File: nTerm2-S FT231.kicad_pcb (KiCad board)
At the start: 2 copper layers, 147.3 x 55.9 mm, 121 parts, among them J1 VGA, J2 Keyboard, J3 Mouse, J4 Line-out/Speaker, J5 RS-232 V.24, J6 USB_C_Receptacle_USB2.0_16P, J7 Line-out/Speaker, K1 IM41 3V, K2 IM41 3V, K3 IM41 3V, Q1 BC817, Q2 BC817, Q3 BC817, Q4 BC817, Q5 BC817, Q6 BC817, Q7 BC817, Q8 BC817, SW1 IO0, SW2 RESET, SW3 DEFAULTS, U1 ESP32-WROOM-32, U2 LM386, U3 MAX3232E, U4 DS2417, U5 NCP1117-3.3_SOT223, U6 USBLC6-2SC6, U7 FT231XS, Y1 32.768MHz

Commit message: Exported library and footprints to project local library for distribution.
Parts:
- C1, C25, C26, C27: footprint Capacitor_SMD:CP_Elec_6.3x7.7 -> Library:CP_Elec_6.3x7.7
- C10, C11, C12, C14, C17, C19, C21, C8, C9: footprint Capacitor_Tantalum_SMD:CP_EIA-3216-18_Kemet-A_Pad1.58x1.35mm_HandSolder -> Library:CP_EIA-3216-18_Kemet-A_Pad1.58x1.35mm_HandSolder
- C13, C18: footprint Capacitor_Tantalum_SMD:CP_EIA-6032-28_Kemet-C_Pad2.25x2.35mm_HandSolder -> Library:CP_EIA-6032-28_Kemet-C_Pad2.25x2.35mm_HandSolder
- C15, C16, C22, C24, C28, C29, C30, C31, C32, C33, C4, C5, C6, C7: footprint Capacitor_SMD:C_0603_1608Metric_Pad1.08x0.95mm_HandSolder -> Library:C_0603_1608Metric_Pad1.08x0.95mm_HandSolder
- C2: footprint Capacitor_SMD:CP_Elec_5x5.4 -> Library:CP_Elec_5x5.4
- C20: footprint Capacitor_Tantalum_SMD:CP_EIA-3528-21_Kemet-B_Pad1.50x2.35mm_HandSolder -> Library:CP_EIA-3528-21_Kemet-B_Pad1.50x2.35mm_HandSolder
- C23: footprint Capacitor_Tantalum_SMD:CP_EIA-7343-30_AVX-N_Pad2.25x2.55mm_HandSolder -> Library:CP_EIA-7343-30_AVX-N_Pad2.25x2.55mm_HandSolder
- C3: footprint Capacitor_SMD:C_0805_2012Metric_Pad1.18x1.45mm_HandSolder -> Library:C_0805_2012Metric_Pad1.18x1.45mm_HandSolder
- D10, D6, D8, D9: footprint Diode_SMD:D_SOD-123 -> Library:D_SOD-123
- D11, D12: footprint Sporos_Tech_Footprints:DIALIGHT_LED_3MM_DOUBLE -> Library:DIALIGHT_LED_3MM_DOUBLE
- D3: footprint Diode_SMD:Nexperia_CFP3_SOD-123W -> Library:Nexperia_CFP3_SOD-123W
- D4: footprint Sporos_Tech_Footprints:DIALIGHT_LED_3MM_SINGLE -> Library:DIALIGHT_LED_3MM_SINGLE
- E1: footprint Sporos_Tech_Footprints:Gold Cap V-Type -> Library:Gold Cap V-Type
- H1, H2, H3, H4, H5, H6: footprint MountingHole:MountingHole_3.2mm_M3 -> Library:MountingHole_3.2mm_M3
- J1: footprint Sporos_Tech_Footprints:DSUB-15-HD_Female_Horizontal_P2.29x1.98mm_EdgePinOffset8.35mm_Housed_MountingHolesOffset10.89mm -> Library:DSUB-15-HD_Female_Horizontal_P2.29x1.98mm_EdgePinOffset8.35mm_Housed_MountingHolesOffset10.89mm
- J2, J3: footprint Custom_Footprints:Connector_Mini-DIN_Female_6Pin_2rows -> Library:Connector_Mini-DIN_Female_6Pin_2rows
- J4: footprint Sporos_Tech_Footprints:Jack_3.5mm_Ledino_KB3SPRS_Horizontal-alt -> Library:Jack_3.5mm_Ledino_KB3SPRS_Horizontal-alt
- J5: footprint Sporos_Tech_Footprints:DSUB-9_Male_Horizontal_P2.77x2.84mm_EdgePinOffset4.94mm_Housed_MountingHolesOffset7.48mm -> Library:DSUB-9_Male_Horizontal_P2.77x2.84mm_EdgePinOffset4.94mm_Housed_MountingHolesOffset7.48mm
- J6: footprint Sporos_Tech_Footprints:USB_C_Receptacle_Molex_213716-0001 -> Library:USB_C_Receptacle_Molex_213716-0001
- J7: footprint Connector_PinHeader_2.54mm:PinHeader_1x02_P2.54mm_Vertical -> Library:PinHeader_1x02_P2.54mm_Vertical
- JP1: footprint Jumper:SolderJumper-3_P1.3mm_Open_RoundedPad1.0x1.5mm_NumberLabels -> Library:SolderJumper-3_P1.3mm_Open_RoundedPad1.0x1.5mm_NumberLabels
- K1, K2, K3: footprint Sporos_Tech_Footprints:Relay_DPDT_AXICOM_IMSeries_Gullwing -> Library:Relay_DPDT_AXICOM_IMSeries_Gullwing
- Q1, Q2, Q3, Q4, Q5, Q6, Q7, Q8: footprint Package_TO_SOT_SMD:SOT-23 -> Library:SOT-23
- R1, R10, R11, R12, R13, R14, R15, R16, R17, R18, R19, R2, R20, R21, R22, R23, R24, R25, R26, R27, R28, R29, R3, R30, R31, R32, R33, R34, R35, R36, R37, R38, R39, R4, R40, R41, R42, R43, R5, R6, R7, R8, R9: footprint Resistor_SMD:R_0603_1608Metric_Pad0.98x0.95mm_HandSolder -> Library:R_0603_1608Metric_Pad0.98x0.95mm_HandSolder
- SW1, SW2, SW3: footprint Sporos_Tech_Footprints:SW_Tactile_SPST_Angled_PTS645Vx58-2LFS-alt -> Library:SW_Tactile_SPST_Angled_PTS645Vx58-2LFS-alt
- U1: footprint RF_Module:ESP32-WROOM-32 -> Library:ESP32-WROOM-32
- U2: footprint Package_SO:SOIC-8_3.9x4.9mm_P1.27mm -> Library:SOIC-8_3.9x4.9mm_P1.27mm
- U3: footprint Package_SO:SOIC-16_3.9x9.9mm_P1.27mm -> Library:SOIC-16_3.9x9.9mm_P1.27mm
- U4: footprint Package_SO_J-Lead:TSOC-6_3.76x3.94mm_P1.27mm -> Library:TSOC-6_3.76x3.94mm_P1.27mm
- U5: footprint Package_TO_SOT_SMD:SOT-223-3_TabPin2 -> Library:SOT-223-3_TabPin2
- U6: footprint Package_TO_SOT_SMD:SOT-23-6 -> Library:SOT-23-6
- U7: footprint Package_SO:SSOP-20_3.9x8.7mm_P0.635mm -> Library:SSOP-20_3.9x8.7mm_P0.635mm
- Y1: footprint Crystal:Crystal_C38-LF_D3.0mm_L8.0mm_Horizontal -> Library:Crystal_C38-LF_D3.0mm_L8.0mm_Horizontal

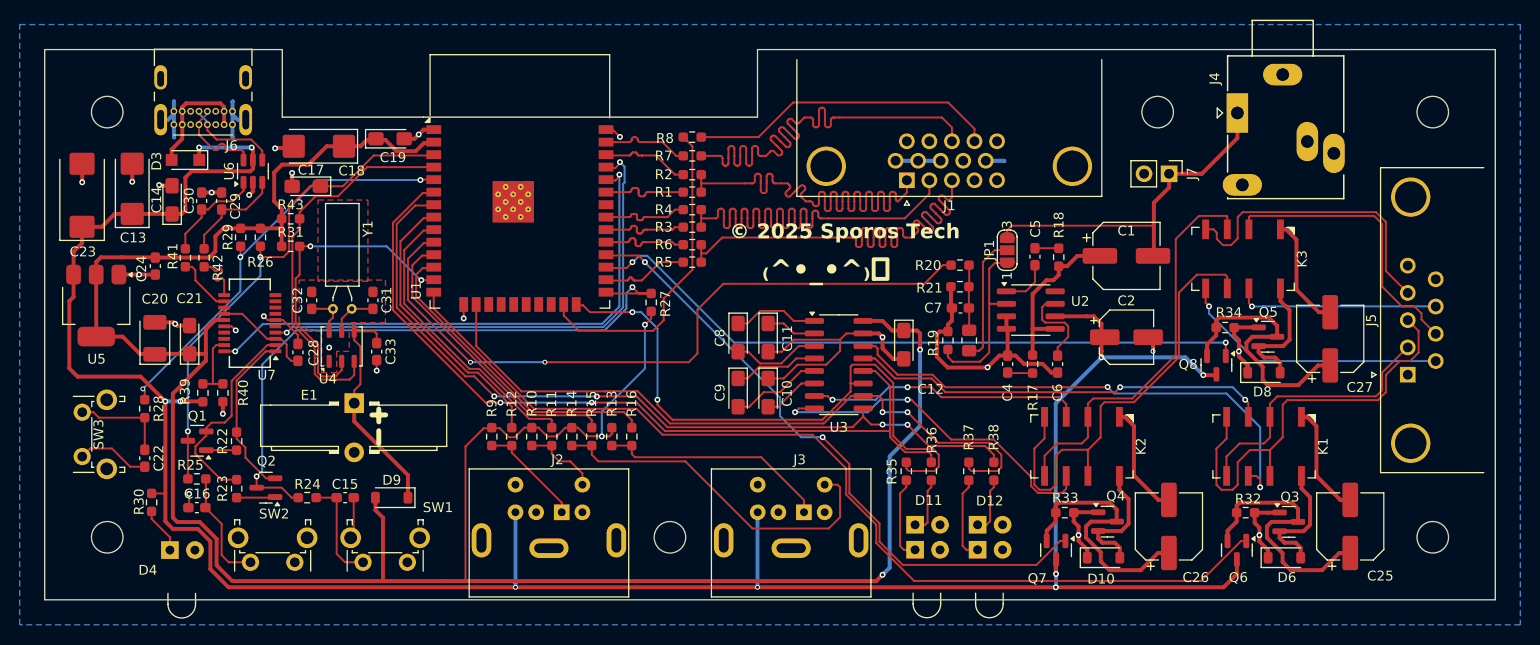
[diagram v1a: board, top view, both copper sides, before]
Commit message: Changed supercap to a CR2032 battery for timekeeping. Exported library. Fixed VGA footprint. Added a few more 3D footprints.
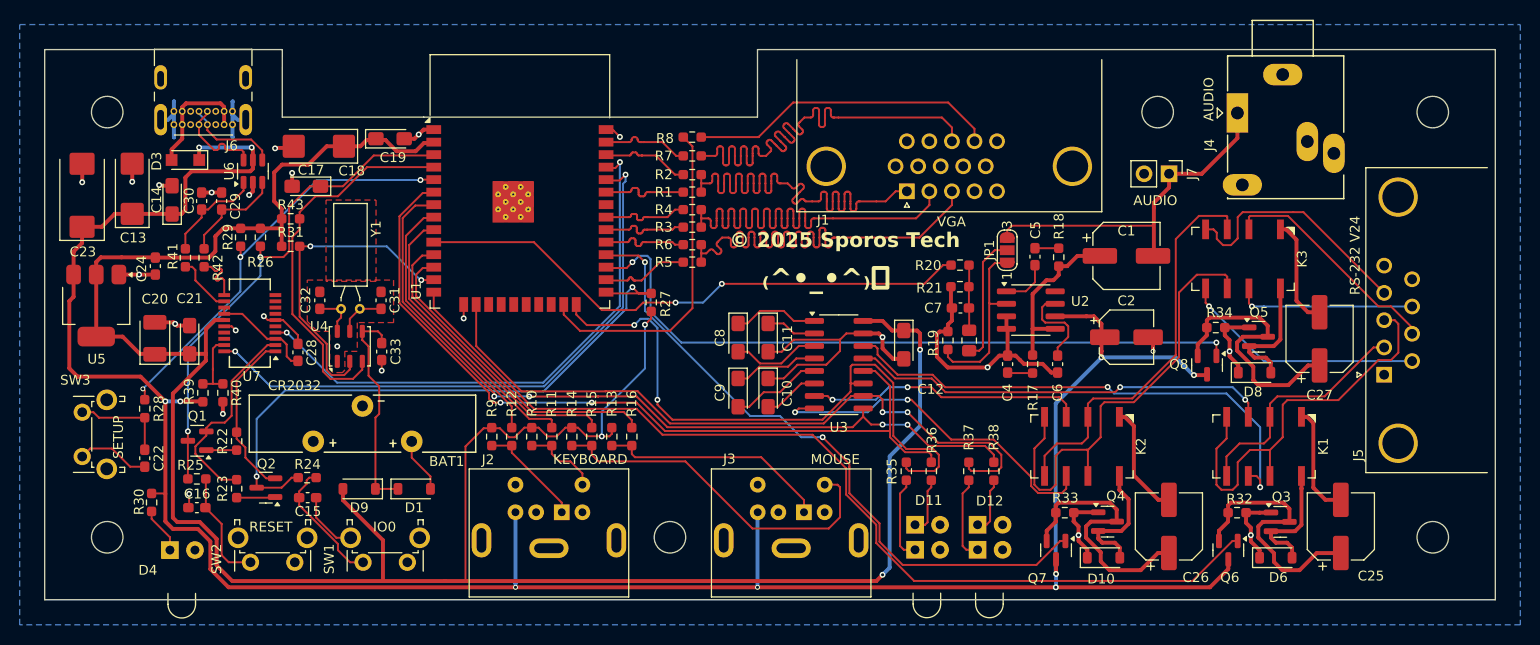
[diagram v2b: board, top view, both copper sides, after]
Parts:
- removed E1: 1.0F, Library:Gold Cap V-Type
- added BAT1: CR2032, nTerm2-S:TE Connectivity CR2032 V, F.Cu at (106.4, 108.2)
- added D1: BAT43W-V, nTerm2-S:D_SOD-123, F.Cu at (111.6, 116.6)
- C1, C25, C26, C27: footprint Library:CP_Elec_6.3x7.7 -> nTerm2-S:CP_Elec_6.3x7.7
- C10, C11, C12, C14, C17, C19, C21, C8, C9: footprint Library:CP_EIA-3216-18_Kemet-A_Pad1.58x1.35mm_HandSolder -> nTerm2-S:CP_EIA-3216-18_Kemet-A_Pad1.58x1.35mm_HandSolder
- C13, C18: footprint Library:CP_EIA-6032-28_Kemet-C_Pad2.25x2.35mm_HandSolder -> nTerm2-S:CP_EIA-6032-28_Kemet-C_Pad2.25x2.35mm_HandSolder
- C15, C16, C22, C24, C28, C29, C30, C31, C32, C33, C4, C5, C6, C7: footprint Library:C_0603_1608Metric_Pad1.08x0.95mm_HandSolder -> nTerm2-S:C_0603_1608Metric_Pad1.08x0.95mm_HandSolder
- C2: footprint Library:CP_Elec_5x5.4 -> nTerm2-S:CP_Elec_5x5.4
- C20: footprint Library:CP_EIA-3528-21_Kemet-B_Pad1.50x2.35mm_HandSolder -> nTerm2-S:CP_EIA-3528-21_Kemet-B_Pad1.50x2.35mm_HandSolder
- C23: footprint Library:CP_EIA-7343-30_AVX-N_Pad2.25x2.55mm_HandSolder -> nTerm2-S:CP_EIA-7343-30_AVX-N_Pad2.25x2.55mm_HandSolder
- C3: footprint Library:C_0805_2012Metric_Pad1.18x1.45mm_HandSolder -> nTerm2-S:C_0805_2012Metric_Pad1.18x1.45mm_HandSolder
- D10, D6, D8, D9: footprint Library:D_SOD-123 -> nTerm2-S:D_SOD-123
- D11, D12: footprint Library:DIALIGHT_LED_3MM_DOUBLE -> nTerm2-S:DIALIGHT_LED_3MM_DOUBLE
- D3: footprint Library:Nexperia_CFP3_SOD-123W -> nTerm2-S:Nexperia_CFP3_SOD-123W
- D4: footprint Library:DIALIGHT_LED_3MM_SINGLE -> nTerm2-S:DIALIGHT_LED_3MM_SINGLE
- H1, H2, H3, H4, H5, H6: footprint Library:MountingHole_3.2mm_M3 -> nTerm2-S:MountingHole_3.2mm_M3
- J1: footprint Library:DSUB-15-HD_Female_Horizontal_P2.29x1.98mm_EdgePinOffset8.35mm_Housed_MountingHolesOffset10.89mm -> nTerm2-S:DSUB-15-HD AssMann HD 15FW
- J2, J3: footprint Library:Connector_Mini-DIN_Female_6Pin_2rows -> nTerm2-S:Connector_Mini-DIN_Female_6Pin_2rows
- J4: footprint Library:Jack_3.5mm_Ledino_KB3SPRS_Horizontal-alt -> nTerm2-S:Jack_3.5mm_Ledino_KB3SPRS_Horizontal-alt
- J5: footprint Library:DSUB-9_Male_Horizontal_P2.77x2.84mm_EdgePinOffset4.94mm_Housed_MountingHolesOffset7.48mm -> nTerm2-S:DSUB-9_Pins_Horizontal_P2.77x2.84mm_EdgePinOffset7.70mm_Housed_MountingHolesOffset9.12mm
- J6: footprint Library:USB_C_Receptacle_Molex_213716-0001 -> nTerm2-S:USB_C_Receptacle_Molex_213716-0001
- J7: footprint Library:PinHeader_1x02_P2.54mm_Vertical -> nTerm2-S:PinHeader_1x02_P2.54mm_Vertical
- JP1: footprint Library:SolderJumper-3_P1.3mm_Open_RoundedPad1.0x1.5mm_NumberLabels -> nTerm2-S:SolderJumper-3_P1.3mm_Open_RoundedPad1.0x1.5mm_NumberLabels
- K1, K2, K3: footprint Library:Relay_DPDT_AXICOM_IMSeries_Gullwing -> nTerm2-S:Relay_DPDT_AXICOM_IMSeries_Gullwing
- Q1, Q2, Q3, Q4, Q5, Q6, Q7, Q8: footprint Library:SOT-23 -> nTerm2-S:SOT-23
- R1, R10, R11, R12, R13, R14, R15, R16, R17, R18, R19, R2, R20, R21, R22, R23, R24, R25, R26, R27, R28, R29, R3, R30, R31, R32, R33, R34, R35, R36, R37, R38, R39, R4, R40, R41, R42, R43, R5, R6, R7, R8, R9: footprint Library:R_0603_1608Metric_Pad0.98x0.95mm_HandSolder -> nTerm2-S:R_0603_1608Metric_Pad0.98x0.95mm_HandSolder
- SW1, SW2, SW3: footprint Library:SW_Tactile_SPST_Angled_PTS645Vx58-2LFS-alt -> nTerm2-S:SW_Tactile_SPST_Angled_PTS645Vx58-2LFS-alt
- U1: footprint Library:ESP32-WROOM-32 -> nTerm2-S:ESP32-WROOM-32
- U2: footprint Library:SOIC-8_3.9x4.9mm_P1.27mm -> nTerm2-S:SOIC-8_3.9x4.9mm_P1.27mm
- U3: footprint Library:SOIC-16_3.9x9.9mm_P1.27mm -> nTerm2-S:SOIC-16_3.9x9.9mm_P1.27mm
- U4: footprint Library:TSOC-6_3.76x3.94mm_P1.27mm -> nTerm2-S:TSOC-6_3.76x3.94mm_P1.27mm
- U5: footprint Library:SOT-223-3_TabPin2 -> nTerm2-S:SOT-223-3_TabPin2
- U6: footprint Library:SOT-23-6 -> nTerm2-S:SOT-23-6
- U7: footprint Library:SSOP-20_3.9x8.7mm_P0.635mm -> nTerm2-S:SSOP-20_3.9x8.7mm_P0.635mm
- Y1: footprint Library:Crystal_C38-LF_D3.0mm_L8.0mm_Horizontal -> nTerm2-S:Crystal_C38-LF_D3.0mm_L8.0mm_Horizontal
- moved C15 3.81 mm to (100.8, 117.5)
- moved D9 3.42 mm to (106.0, 116.6)
- moved J5 2.40 mm to (210.1, 105.0)
- moved R24 2.03 mm to (100.8, 115.4)
- moved C27 1.08 mm to (203.6, 101.3)
- moved C25 0.95 mm to (205.7, 120.4)
- moved Q5 0.95 mm to (197.4, 101.1)
- moved Q8 0.95 mm to (192.2, 104.0)
- moved R34 0.95 mm to (193.0, 100.2)
- moved D8 0.95 mm to (197.0, 104.8)
- moved D6 0.87 mm to (199.1, 123.6)
- moved Q3 0.87 mm to (199.6, 119.9)
- moved Q6 0.87 mm to (194.3, 122.8)
- moved R32 0.87 mm to (195.2, 119.0)
- moved C31 0.82 mm to (108.3, 97.4)
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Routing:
- net AUDIO_PWM: track 72.0 -> 57.3 mm
- net /_RTS: track 29.3 -> 23.2 mm
- net RXD_0: track 55.2 -> 61.1 mm
- net Net-(D1-A): track 0.00 -> 5.62 mm
- net TXD_0: track 51.2 -> 56.7 mm
- net /_DTR: track 30.5 -> 25.2 mm
- net GND: track 140.5 -> 136.6 mm
- net /_RXD: track 27.3 -> 23.8 mm
- net /_DSR: track 27.9 -> 24.9 mm
- net IO0: track 65.7 -> 62.9 mm
- net /_CTS: track 20.9 -> 18.2 mm
- net /_TXD: track 44.5 -> 42.2 mm
- net +3V3: track 255.2 -> 257.5 mm
- net RTS_CTS_OR_DTR_DSR: track 68.5 -> 70.6 mm
- net +5V: track 249.9 -> 247.8 mm
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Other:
- board text added: "AUDIO"
- board text added: "CR2032"
- board text added: "IO0"
- board text added: "KEYBOARD"
- board text added: "MOUSE"
- board text added: "RESET"
- board text added: "RS-232 V24"
- board text added: "SETUP"
- board text added: "VGA"
